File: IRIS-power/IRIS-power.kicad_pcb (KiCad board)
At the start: 2 copper layers, 66.9 x 65 mm, 83 parts, among them J101 Powerpole, J102 PJ-047AH, J801 IRIS_physical, Q21 2N7002, Q61 IRLML6402, U101 TVS1400DRV, U102 TVS1400DRV, U21 MAX17261, U31 TPS2121, U41 TPS55340, U51 TPSM53604, U61 LTC3110, U62 PCA9537, U71 TLV75733PDBV

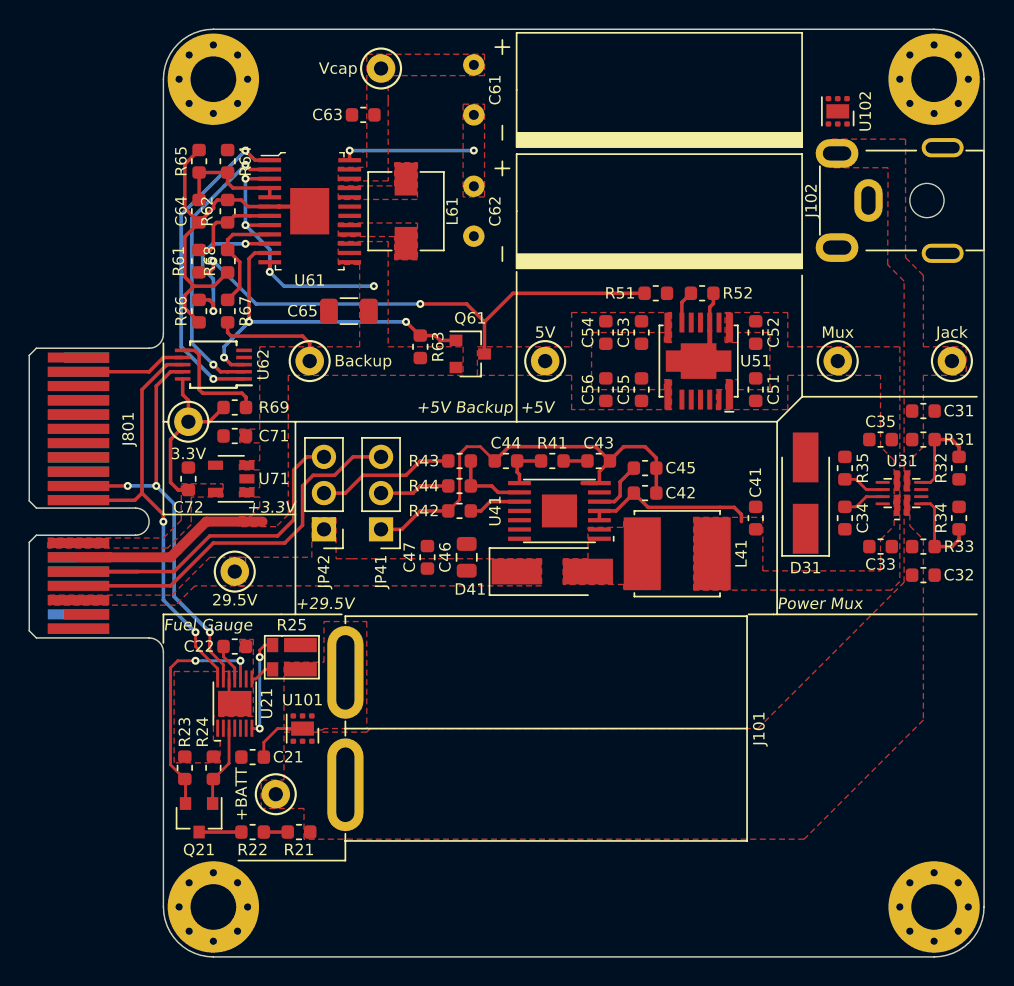
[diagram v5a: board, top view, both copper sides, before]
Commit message: Updated layout
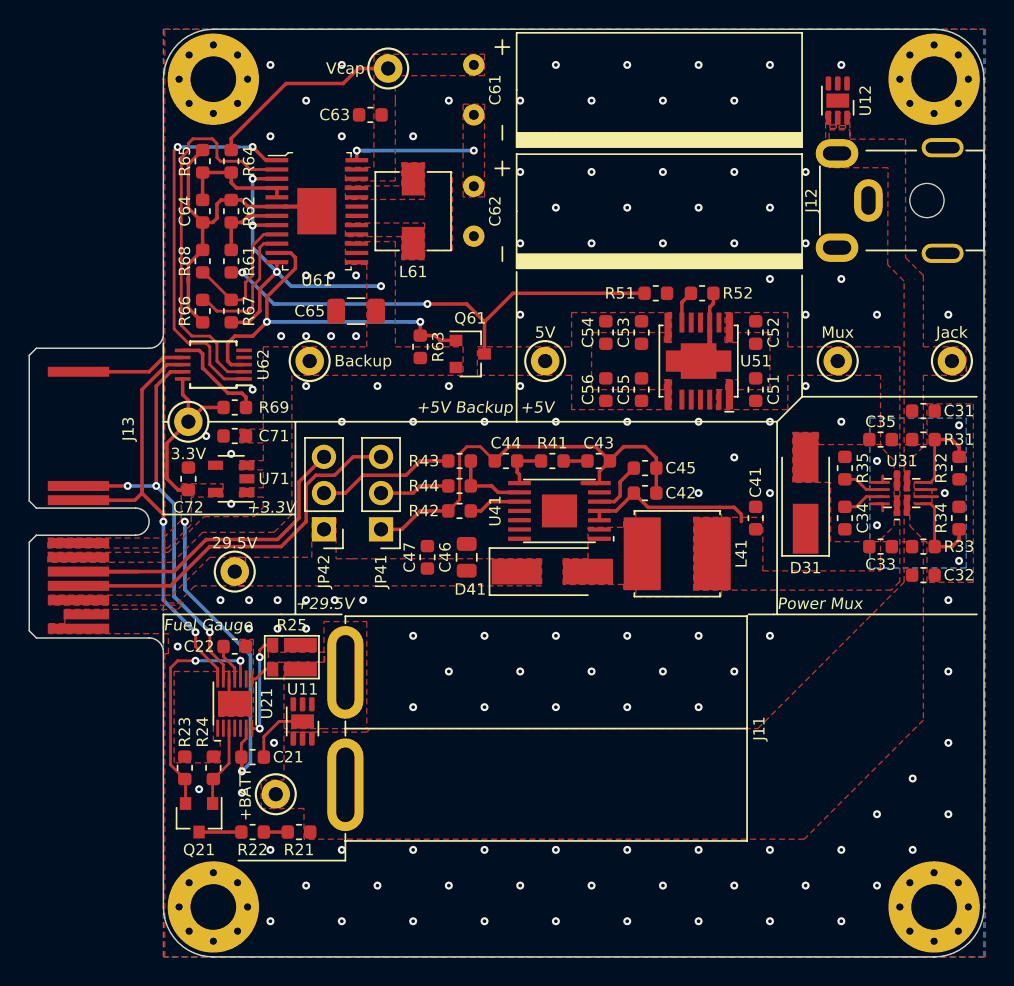
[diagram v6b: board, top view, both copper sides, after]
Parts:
- removed J801: IRIS_physical, star-common-lib:IRIS_Physical
- removed U101, U102: TVS1400DRV, Package_SON:WSON-6-1EP_2x2mm_P0.65mm_EP1x1.6mm
- added J13: IRIS_power_board, star-common-lib:IRIS_Power_Physical, F.Cu at (0.00, 0.00)
- added U11: TVS1400DRV, star-common-lib:WSON-6-1EP_2x2mm_Hand_Solder, F.Cu at (9.75, 48.5)
- added U12: TVS1400DRV, star-common-lib:WSON-6-1EP_2x2mm_Hand_Solder, F.Cu at (47.2, 5.00)
- moved R61 2.25 mm to (4.75, 16.2)
- moved R68 1.75 mm to (2.75, 16.2), turned to 90 degrees
- moved C63 0.50 mm to (14.5, 6.00)
- moved C65 0.50 mm to (13.5, 19.8)
- moved L61 0.50 mm to (17.5, 12.8)
- moved TP61 0.50 mm to (15.8, 2.75)
- moved U61 0.50 mm to (10.8, 12.8)
- moved NT61 0.43 mm to (9.00, 12.4)
- moved C64 0.25 mm to (2.75, 12.8)
- moved R62 0.25 mm to (4.75, 12.8)
- moved R64 0.25 mm to (4.75, 9.25)
- moved R65 0.25 mm to (2.75, 9.25)
- moved R66 0.25 mm to (2.75, 19.8)
- moved R67 0.25 mm to (4.75, 19.8)
- renumbered J101 to J11, J102 to J12
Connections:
- C21 pad 1: /3V Supply/VSYS -> /3V Supply/+3.3V
- U21 pad 6: /3V Supply/VSYS -> /3V Supply/+3.3V
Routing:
- net /3V Supply/+3.3V: track 12.3 -> 35.4 mm, vias 0 -> 2
- net /3V Supply/VSYS: track 41.0 -> 24.6 mm
- net /5V Backup/Vcap: track 0.00 -> 13.8 mm
- net /5V Backup/CAP_OK: track 22.9 -> 31.5 mm
- net /5V Backup/~CMP_OUT: track 20.4 -> 27.2 mm, vias 2 -> 0
- net /Power Mux/GND_P: track 0.00 -> 4.95 mm, vias 0 -> 5
- net /5V Backup/+5V: track 36.7 -> 33.5 mm
- net GNDS: track 23.0 -> 20.7 mm
- net /5V Backup/FB: track 8.02 -> 9.75 mm
- net /5V Backup/DIR: track 6.82 -> 5.32 mm
- net /5V Backup/~CHRG: track 25.9 -> 27.3 mm, vias 3 -> 2
- net /5V Backup/PROG: track 10.9 -> 9.65 mm, vias 2 -> 0
- net Net-(R69-Pad2): track 7.95 -> 7.10 mm
- net /Edge Connector/FB_HV_P: track 26.8 -> 26.2 mm
- net GND: vias 0 -> 130
- added copper zone on B.Cu, net /Power Mux/GND_P
- added copper zone on F.Cu, net /Power Mux/GND_P
- added copper zone on B.Cu, net GND
- added copper zone on F.Cu, net GND

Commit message: Added some 3D models
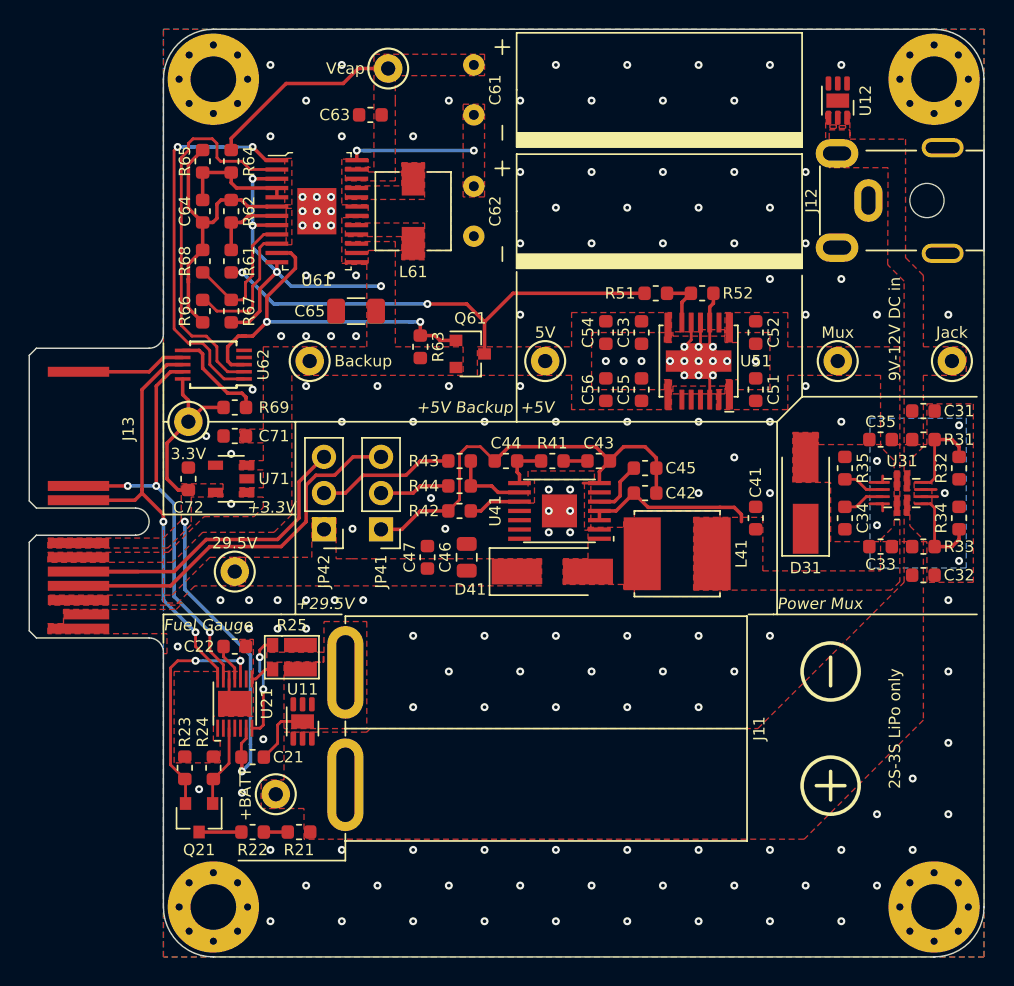
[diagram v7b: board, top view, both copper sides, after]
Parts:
- moved NT61 2.22 mm to (6.78, 12.4)
- moved NT51 1.79 mm to (38.3, 19.8)
- moved NT41 0.80 mm to (30.6, 31.4), turned to 270 degrees
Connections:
- NT41 pad 1: GND -> /HV Supply/AGND
- NT41 pad 2: /HV Supply/AGND -> GND
- U41 pad 7: /HV Supply/AGND -> GND
- U51 pad 12: /5V Supply/AGND -> GND
- U61 pad 6: GNDS -> GND
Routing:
- net GND: track 0.00 -> 8.38 mm, vias 130 -> 163
- net GNDS: track 20.7 -> 19.0 mm
- net /5V Supply/FB: track 2.31 -> 3.99 mm
- net /5V Supply/AGND: track 2.16 -> 1.07 mm
- net /HV Supply/AGND: track 29.9 -> 29.1 mm
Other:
- board text added: "2S-3S LiPo only"
- board text added: "9V-12V DC in"

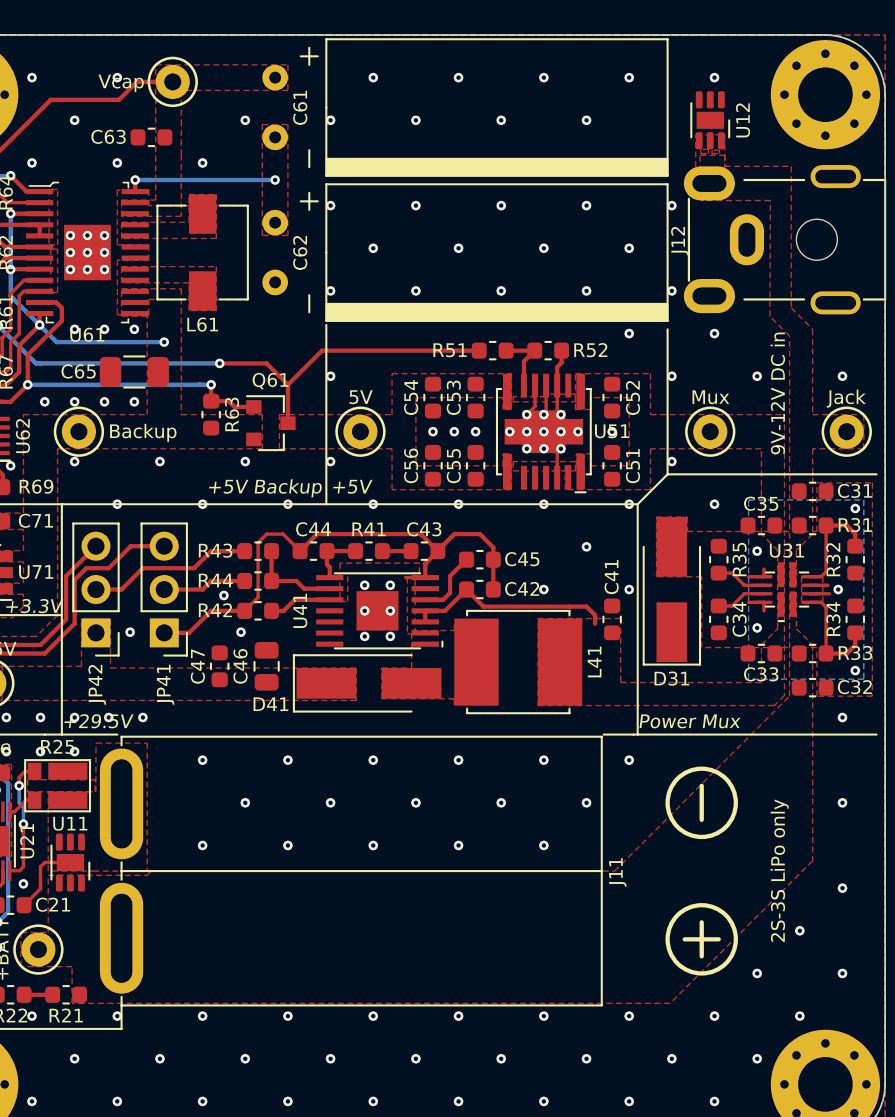
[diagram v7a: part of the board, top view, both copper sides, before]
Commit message: Updated 3D models
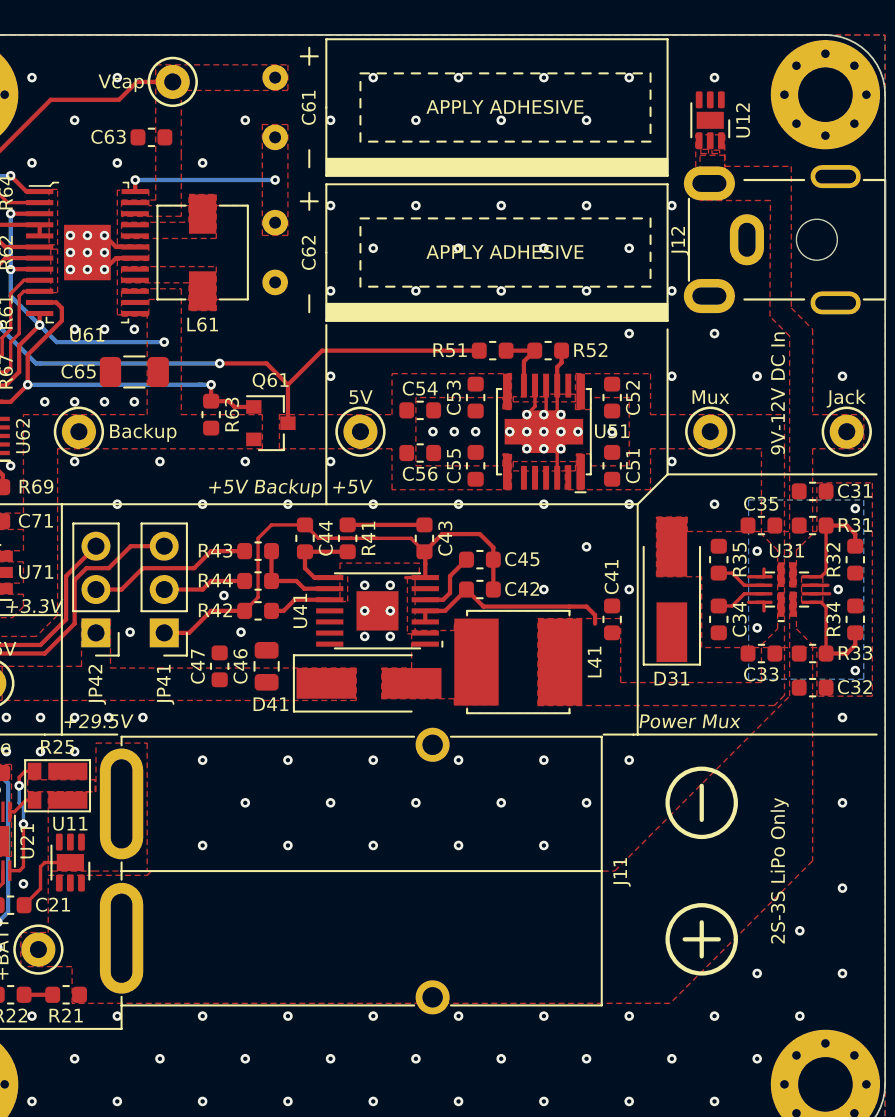
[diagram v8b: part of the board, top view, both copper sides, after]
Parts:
- moved R41 1.46 mm to (26.0, 29.5), turned to 90 degrees
- moved C54 1.06 mm to (30.2, 22.0), turned to 0 degrees
- moved C56 1.06 mm to (30.2, 24.5), turned to 0 degrees
- moved C44 0.90 mm to (23.5, 29.5), turned to 90 degrees
- moved C43 0.75 mm to (30.5, 29.5), turned to 270 degrees
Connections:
- J11 pad 1: /Fuel Gauge/-BATT -> /Fuel Gauge/+BATT
- J11 pad 2: /Fuel Gauge/+BATT -> /Fuel Gauge/-BATT
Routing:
- net GND: track 8.38 -> 12.5 mm
- net Net-(C43-Pad1): track 1.67 -> 4.50 mm
- net /HV Supply/COMP: track 3.29 -> 5.14 mm
- net /HV Supply/AGND: track 29.1 -> 29.8 mm
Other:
- board text added: "2S-3S LiPo Only"
- board text added: "9V-12V DC In"
- board text removed: "2S-3S LiPo only"
- board text removed: "9V-12V DC in"
